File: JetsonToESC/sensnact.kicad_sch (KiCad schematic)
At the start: 8 parts, among them U2 DS18B20

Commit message: Start On this Branch
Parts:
- added C3: 100nF, Capacitor_SMD:C_0805_2012Metric_Pad1.18x1.45mm_HandSolder, symbol Device:C_Small
- added R13: 4K7, Resistor_SMD:R_0603_1608Metric, symbol Device:R
- added U5: ACS759xCB-100B-PFF, Sensor_Current:Allegro_CB_PFF, symbol Sensor_Current:ACS759xCB-100B-PFF
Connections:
- net 3V3: now also C3.2, U5.1 (VCC)
- net GND: now also C3.1, U5.2 (GND)
- new net: R13.2, U5.3 (VIOUT)
- new net CURRENT_SENSE: R13.1
- new net VBAT_IN: U5.4 (IP+)
- new net VBAT_OUT: U5.5 (IP-)
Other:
- moved on the sheet: C2, OC2, R1, R12, R2, R3, R9, U2

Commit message: Work on current sense and io expansion branch
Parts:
- C2: footprint Capacitor_SMD:C_0805_2012Metric_Pad1.18x1.45mm_HandSolder -> Capacitor_SMD:C_0603_1608Metric
- R2, R3: footprint Resistor_SMD:R_0805_2012Metric_Pad1.20x1.40mm_HandSolder -> Resistor_SMD:R_0603_1608Metric
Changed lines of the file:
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@@
 			)
 		)
-		(property "Footprint" "Resistor_SMD:R_0805_2012Metric_Pad1.20x1.40mm_HandSolder"
+		(property "Footprint" "Resistor_SMD:R_0603_1608Metric"
 			(at 55.88 46.99 0)
 			(effects
@@
 			)
 		)
-		(property "Footprint" "Resistor_SMD:R_0805_2012Metric_Pad1.20x1.40mm_HandSolder"
+		(property "Footprint" "Resistor_SMD:R_0603_1608Metric"
 			(at 55.88 36.83 0)
 			(effects
@@
 			)
 		)
-		(property "Footprint" "Capacitor_SMD:C_0805_2012Metric_Pad1.18x1.45mm_HandSolder"
+		(property "Footprint" "Capacitor_SMD:C_0603_1608Metric"
 			(at 48.26 46.99 0)
 			(effects

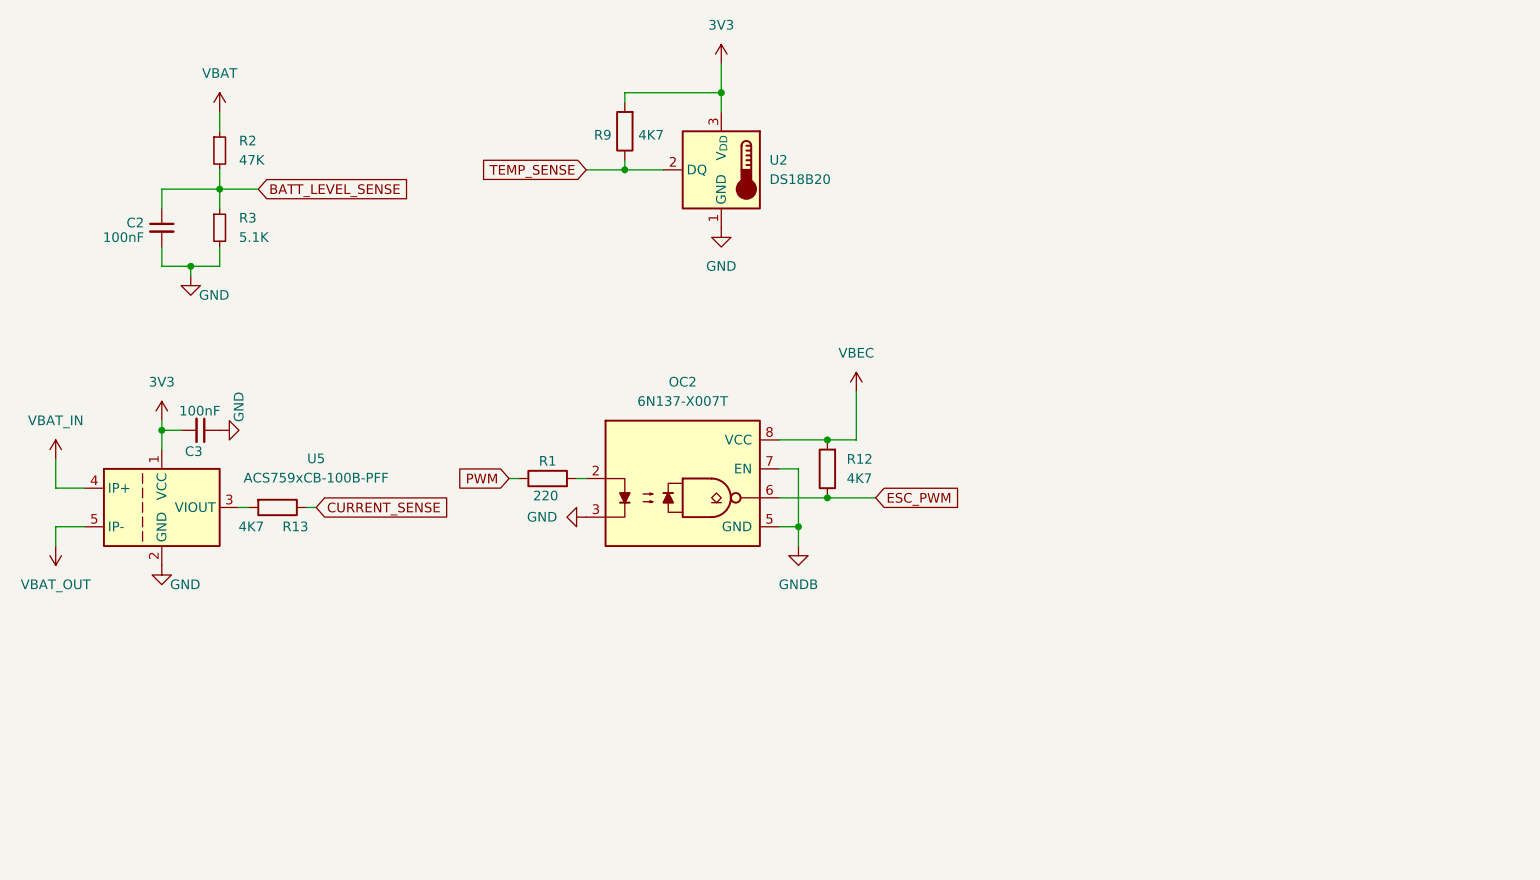
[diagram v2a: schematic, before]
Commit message: Updated routing for IO Expander and Hall Sensor
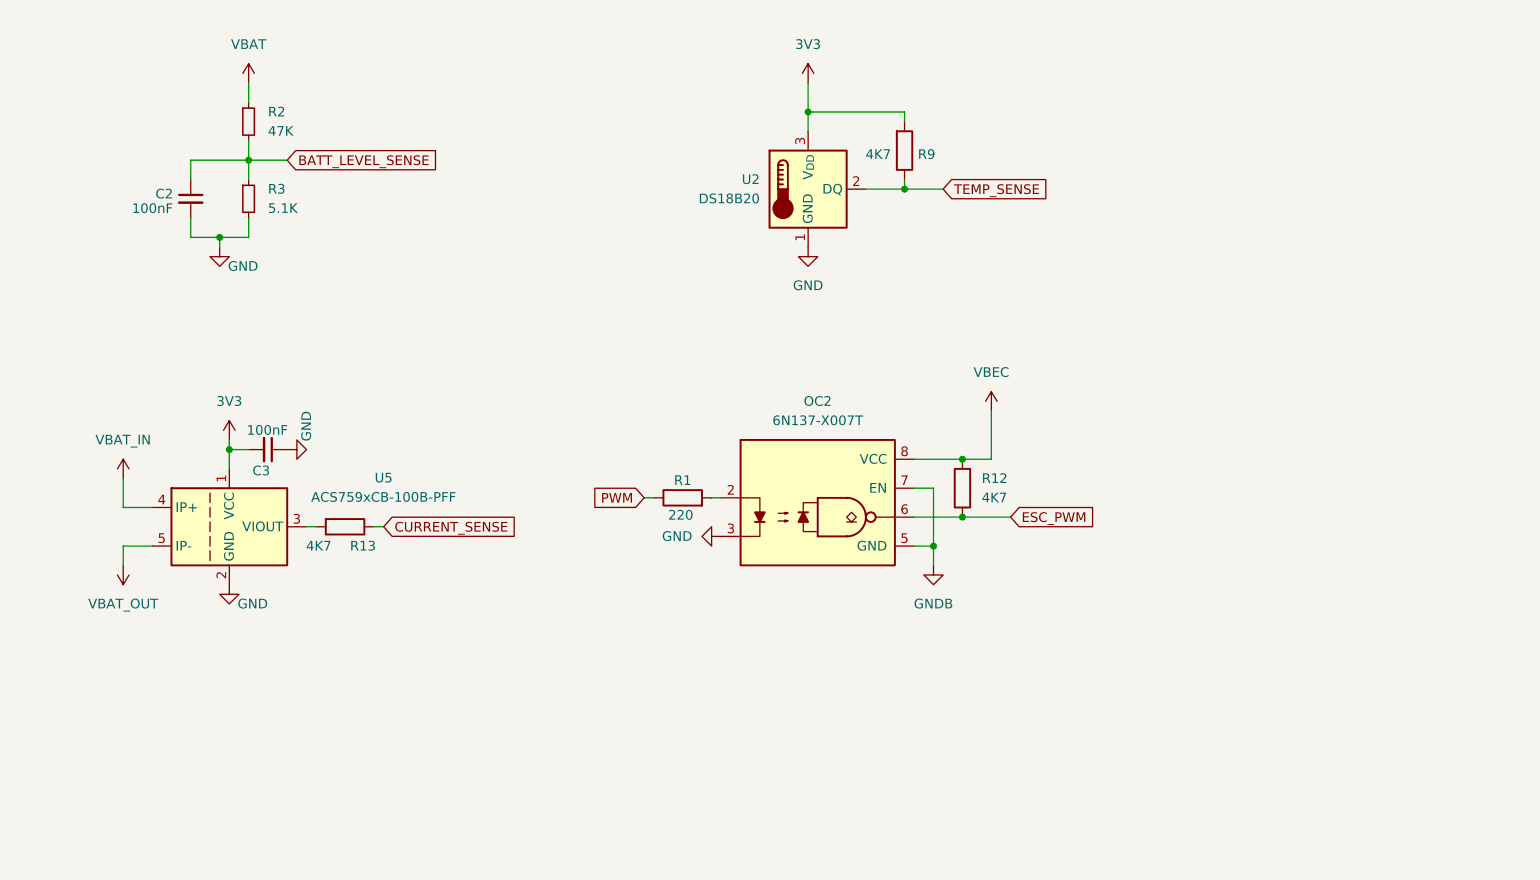
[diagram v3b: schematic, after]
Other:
- moved on the sheet: C2, C3, OC2, R1, R12, R13, R2, R3, R9, U2, U5

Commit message: Edit around current sensor
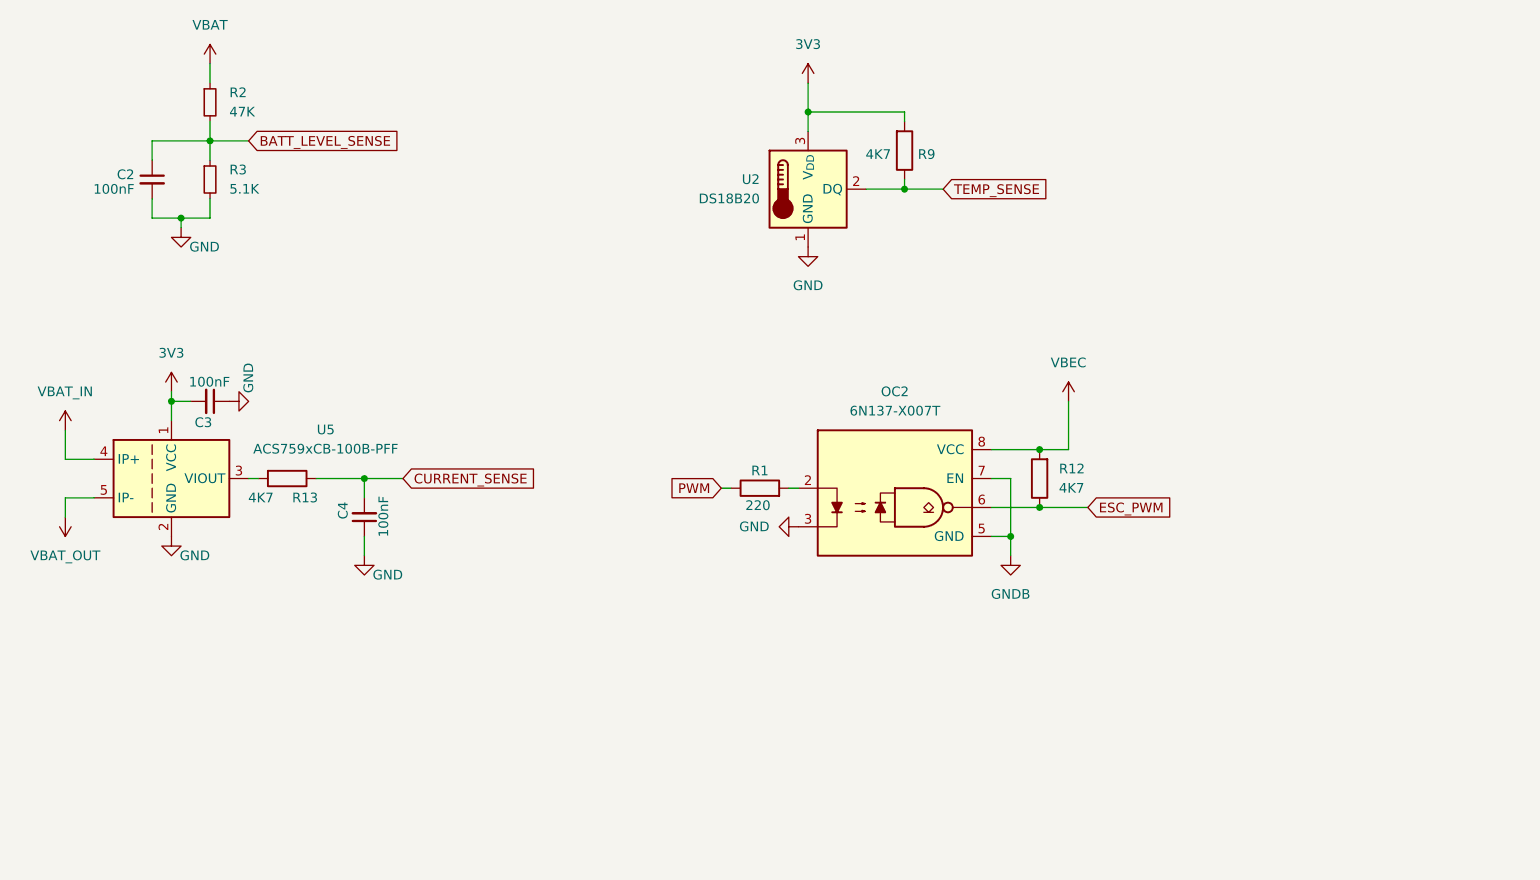
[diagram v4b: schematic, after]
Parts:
- added C4: 100nF, Capacitor_SMD:C_0805_2012Metric_Pad1.18x1.45mm_HandSolder, symbol Device:C_Small
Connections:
- net CURRENT_SENSE: now also C4.2
- net GND: now also C4.1
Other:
- moved on the sheet: C2, C3, OC2, R1, R12, R13, R2, R3, U5

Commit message: Design and routing done
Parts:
- U5: value ACS759xCB-100B-PFF -> ACS759ECB-200B-PFF-T
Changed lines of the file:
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@@
 			)
 		)
-		(property "Value" "ACS759xCB-100B-PFF"
+		(property "Value" "ACS759ECB-200B-PFF-T"
 			(at 69.85 76.1298 0)
 			(effects
@@
 			)
 		)
-		(property "Description" "±100A Bidirectional Hall-Effect Current Sensor, +3.3V supply, 13.2mV/A, CB-5 PFF"
+		(property "Description" "±200A Bidirectional Hall-Effect Current Sensor, +3.3V supply, 6.6mV/A, CB-5 PFF"
 			(at 49.53 80.01 0)
 			(effects

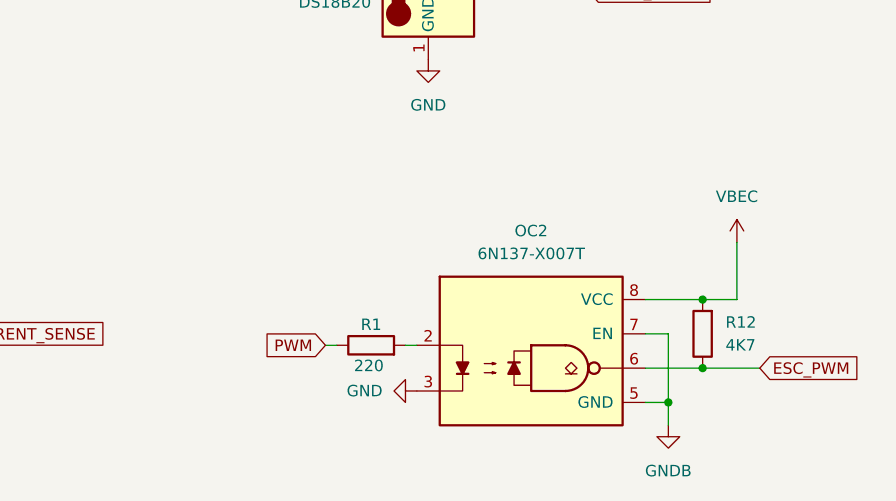
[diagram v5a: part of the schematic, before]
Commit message: Fix on opto en output, now properly wired
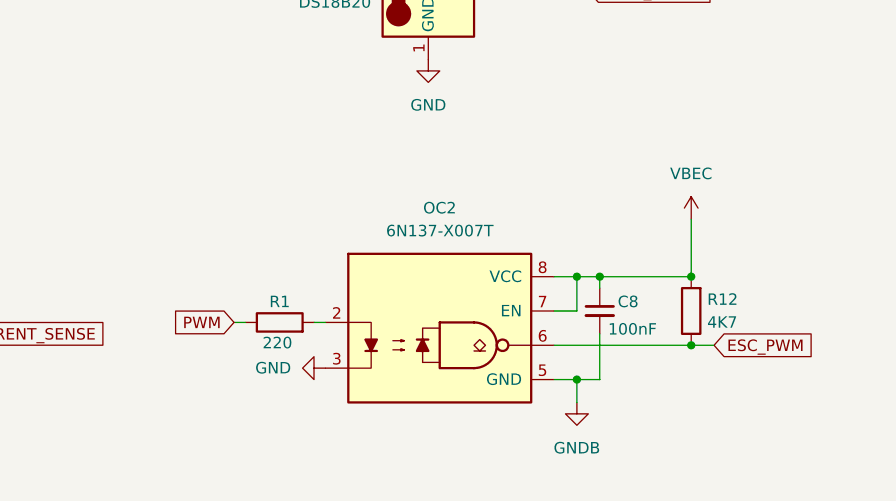
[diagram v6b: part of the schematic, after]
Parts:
- added C8: 100nF, Capacitor_SMD:C_0603_1608Metric, symbol Device:C_Small
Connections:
- net GNDB: now also C8.2; no longer OC2.7 (EN)
- net VBEC: now also OC2.7 (EN), C8.1
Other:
- moved on the sheet: OC2, R1, R12

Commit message: Updated for v2.0, almost complete
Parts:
- removed C8: 100nF, Capacitor_SMD:C_0603_1608Metric, symbol Device:C_Small
- removed OC2: 6N137-X007T, PCM_Package_DIP_AKL:SMDIP-8_W9.53mm, symbol PCM_Optocoupler_Logic_AKL:6N137-X007T
- removed R1: 220, Resistor_SMD:R_0603_1608Metric, symbol Device:R
- removed R12: 4K7, Resistor_SMD:R_0603_1608Metric, symbol Device:R
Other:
- moved on the sheet: C2, C3, C4, R13, R2, R3, R9, U2, U5
